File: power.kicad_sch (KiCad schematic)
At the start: 36 parts, among them J1 39281023, J7 39281023, J8 675031020, U1 AMS1117-3.3, U5 TPS62933, U6 TPS62933

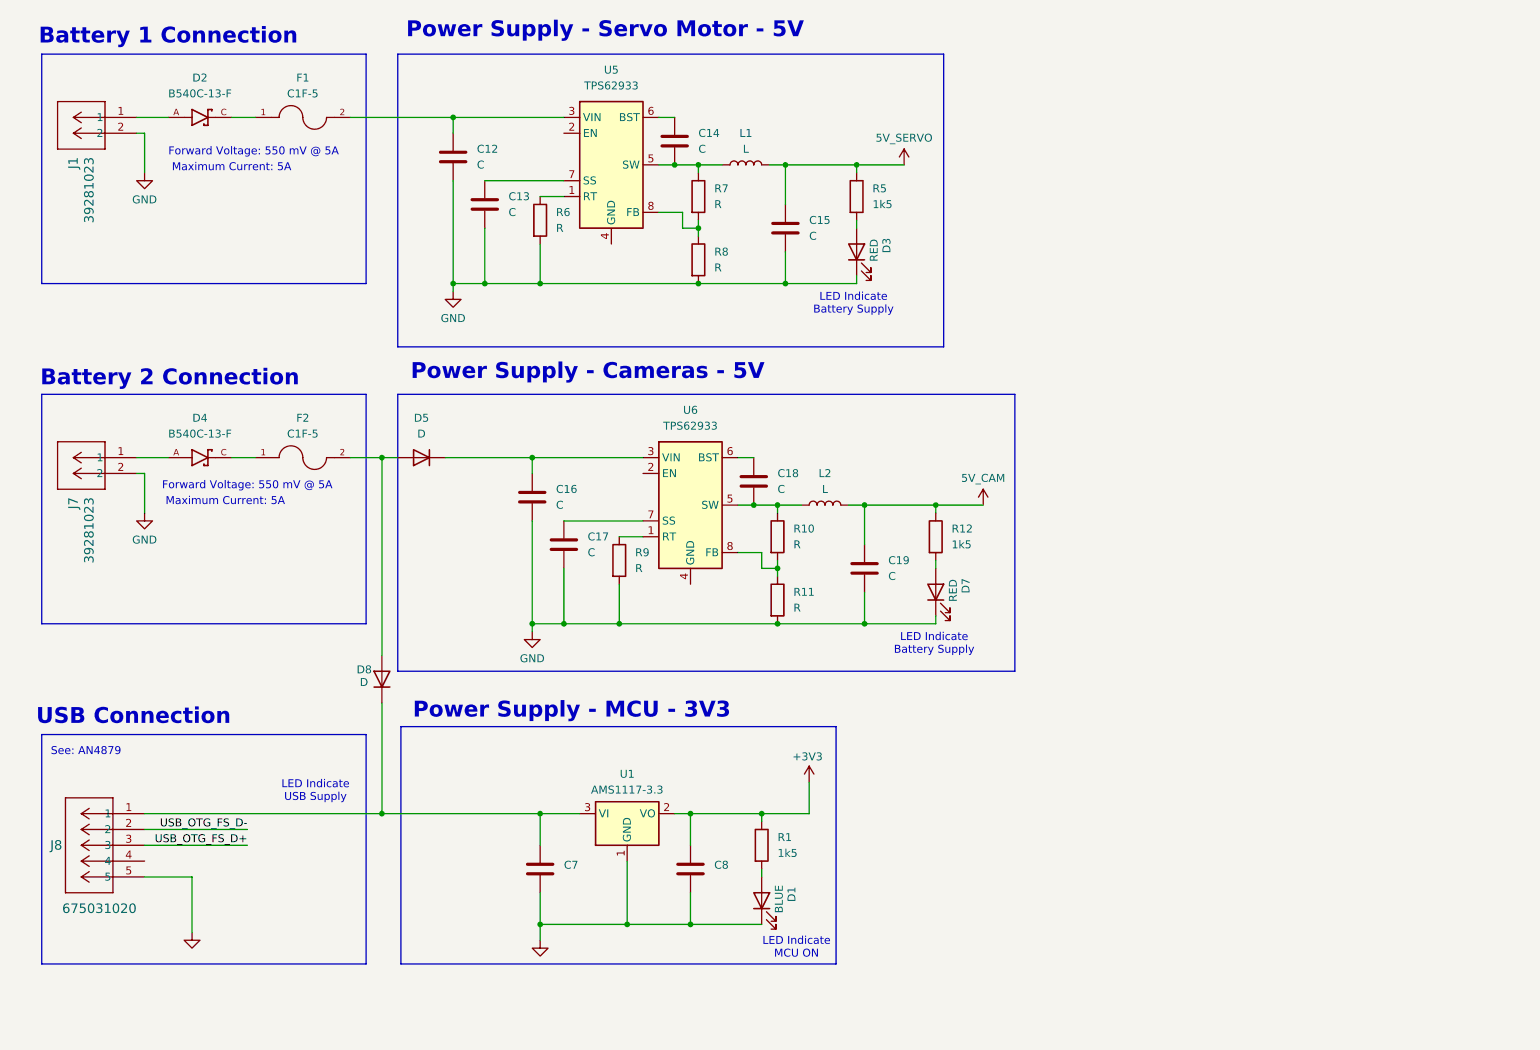
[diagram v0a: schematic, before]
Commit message: Remove redundant diode for camera supply
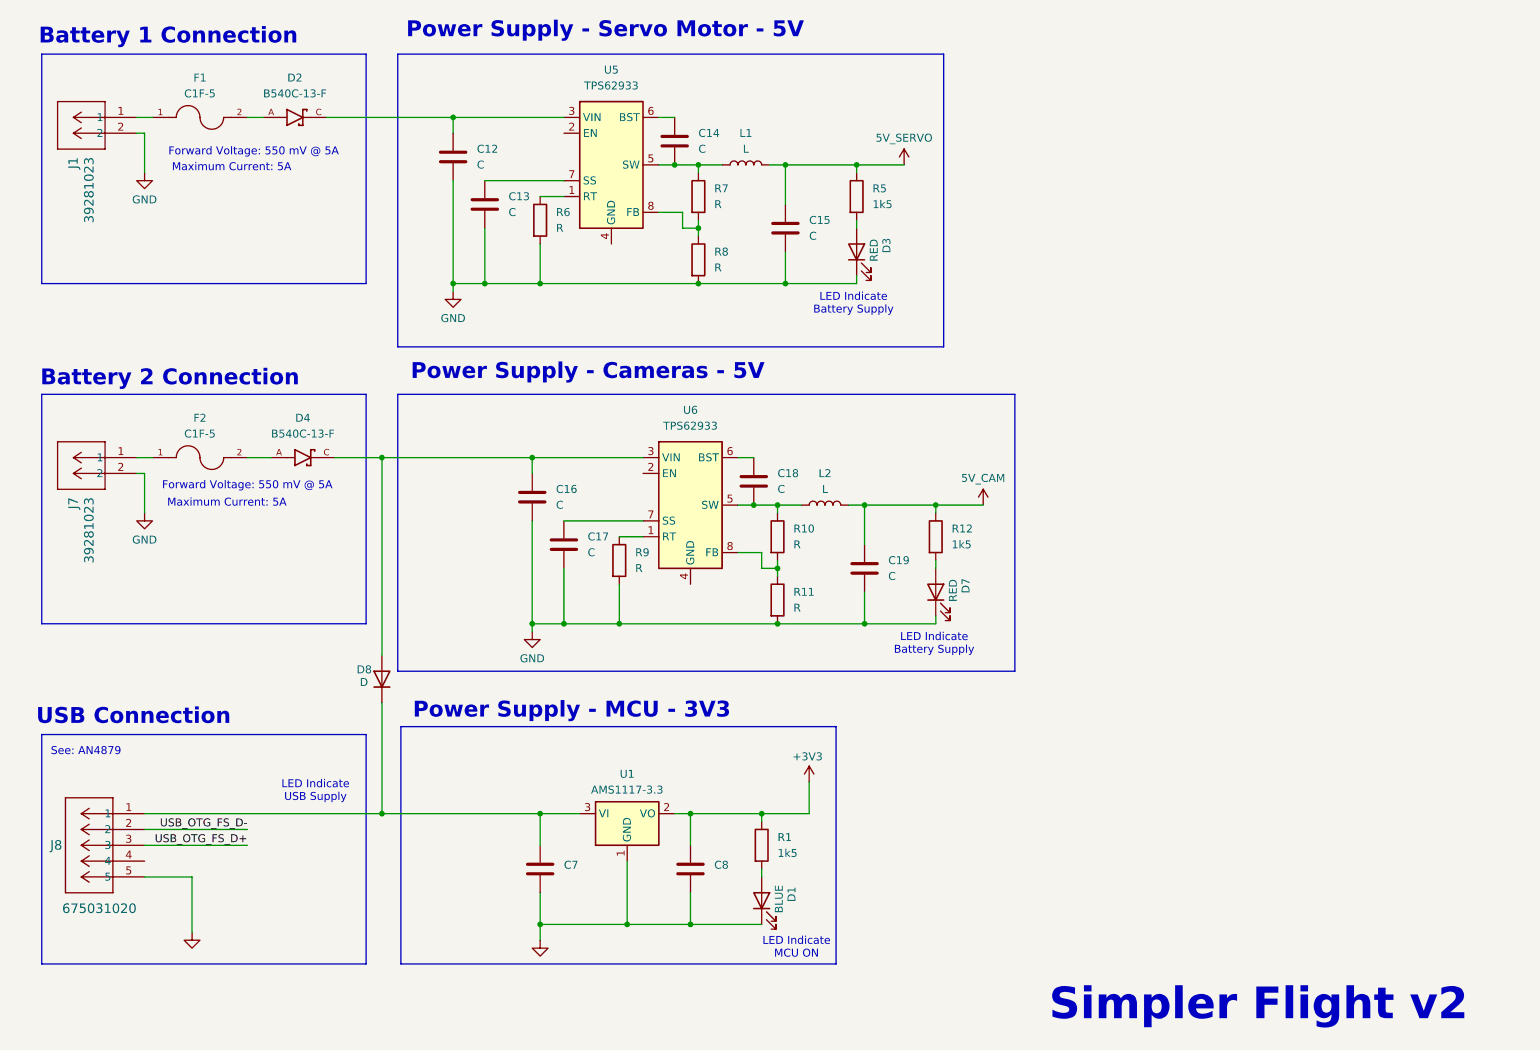
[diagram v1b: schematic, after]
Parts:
- removed D5: D, symbol Device:D
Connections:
- net at J7.1: now also F2.1; no longer D4.A
- net at C16.1, U6.3 (VIN): now also D4.C, D8.2 (A)
- net at D2.A: now also F1.2; no longer J1.1
- net at D2.C: now also C12.1, U5.3 (VIN); no longer F1.1
- net at F2.2: now also D4.A; no longer D8.2 (A)
- new net: F1.1, J1.1
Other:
- note added: "Simpler Flight v2"
- company: (none) -> Lulu Systems
- title: (none) -> Power System
- moved on the sheet: D2, D4, F1, F2

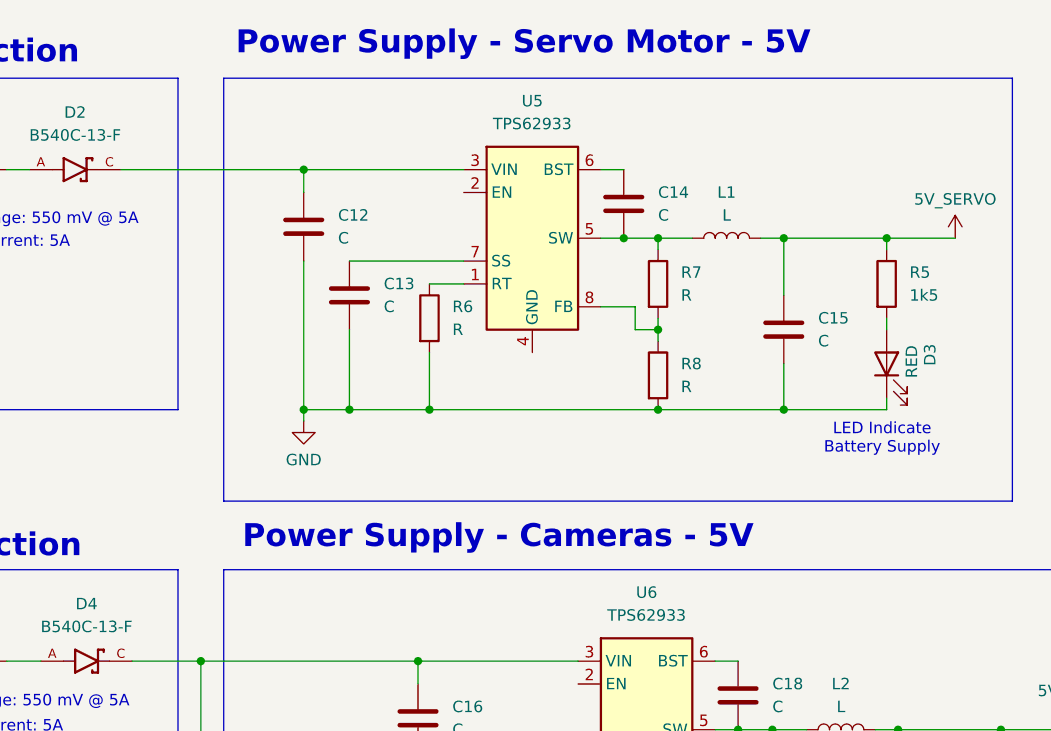
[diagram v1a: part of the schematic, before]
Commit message: Upload architecture diagram, start sensor schematic, add simulation files
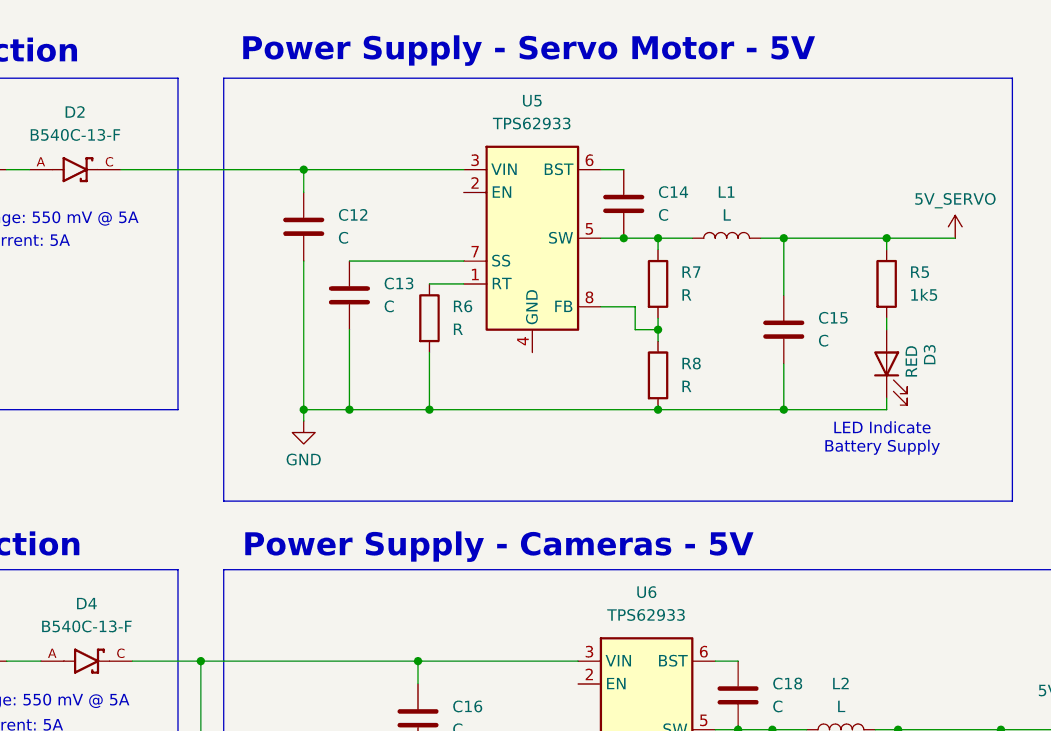
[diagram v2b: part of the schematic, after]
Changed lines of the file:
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@@
 	(text "Power Supply - Servo Motor - 5V"
 		(exclude_from_sim no)
-		(at 109.474 17.78 0)
+		(at 109.982 18.542 0)
 		(effects
 			(font
@@
 	(text "Power Supply - Cameras - 5V"
 		(exclude_from_sim no)
-		(at 106.68 72.644 0)
+		(at 106.68 73.66 0)
 		(effects
 			(font

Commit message: Commit
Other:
- title: Power System -> Power 
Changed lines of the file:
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@@
 	(paper "A4")
 	(title_block
-		(title "Power System")
+		(title "Power ")
 		(company "Lulu Systems")
 	)

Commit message: addecd stuff
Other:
- note added: "LED Indicate Battery Supply to Cameras"
- note added: "LED Indicate Battery Supply to Servo"
- note removed: "LED Indicate Battery Supply"
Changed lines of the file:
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@@
 		)
 	)
-	(text "LED Indicate \nBattery Supply\n\n"
+	(text "LED Indicate \nBattery Supply\nto Cameras"
 		(exclude_from_sim no)
 		(at 162.306 117.348 0)
@@
 		)
 	)
-	(text "LED Indicate \nBattery Supply\n\n"
+	(text "LED Indicate \nBattery Supply\nto Servo"
 		(exclude_from_sim no)
 		(at 149.352 62.738 0)
@@
 			"AAAAAAAAAAAAAAAAAAAAAAAAAAAAAAAAAAAAAAAAAAAAAAAAAAAAAAAAAAAAAAAAAAAAAAAAAAAA"
 			"AAAAAAAAAAAAAAAAAAAAAAAAAAAAAAAAAAAAAAAAAAAAAAAAAAAAAAAAAAAAAAAAAAAAAAAAAAAA"
+			"AAAAAAAAAAAAAAAAAAAAAAAAAAAAAAAAAAAAAAAAAAAAAAAAAAAAAAAAAAAAAAAAAAAAAAAAAAAA"
+			"AAAAAAAAAAAAAAAAAAAAAAAAAAAAAAAAAAAAAAAAAAAAAAAAAAAAAAAAAAAAAAAAAAAAAAAAAAAA"
+			"AAAAAAAAAAAAAAAAAAAAAAAAAAAAAAAAAAAAAAAAAAAAAAAAAAAAAAAAAAAAAAAAAAAAAAAAAAAA"
+			"AAAAAAAAAAAAAAAAAAAAAAAAAAAAAAAAAAAAAAAAAAAAAAAAAAAAAAAAAAAAAAAAAAAAAAAAAAAA"
+			"AAAAAAAAAAAAAAAAAAAAAAAAAAAAAAAAAAAAAAAAAAAAAAAAAAAAAAAAAAAAAAAAAAAAAAAAAAAA"
+			"AAAAAAAAAAAAAAAAAAAAAAAAAAAAAAAAAAAAAAAAAAAAAAAAAAAAAAAAAAAAAAAAAAAAAAAAAAAA"
+			"AAAAAAAAAAAAAAAAAAAAAAAAAAAAAAAAAAAAAAAAAAAAAAAAAAAAAAAAAAAAAAAAAAAAAAAAAAAA"
+			"AAAAAAAAAAAAAAAAAAAAAAAAAAAAAAAAAAAAAAAAAAAAAAAAAAAAAAAAAAAAAAAAAAAAAAAAAAAA"
+			"AAAAAAAAAAAAAAAAAAAAAAAAAAAAAAAAAAAAAAAAAAAAAAAAAAAAAAAAAAAAAAAAAAAAAAAAAAAA"
+			"AAAAAAAAAAAAAAAAAAAAAAAAAAAAAAAAAAAAAAAAAAAAAAAAAAAAAAAAAAAAAAAAAAAAAAAAAAAA"
+			"AAAAAAAAAAAAAAAAAAAAAAAAAAAAAAAAAAAAAAAAAAAAAAAAAAAAAAAAAAAAAAAAAAAAAAAAAAAA"
+			"AAAAAAAAAAAAAAAAAAAAAAAAAAAAAAAAAAAAAAAAAAAAAAAAAAAAAAAAAAAAAAAAAAAAAAAAAAAA"
+			"AAAAAAAAAAAAAAAAAAAAAAAAAAAAAAAAAAAAAAAAAAAAAAAAAAAAAAAAAAAAAAAAAAAAAAAAAAAA"
+			"AAAAAAAAAAAAAAAAAAAAAAAAAAAAAAAAAAAAAAAAAAAAAAAAAAAAAAAAAAAAAAAAAAAAAAAAAAAA"
+			"AAAAAAAAAAAAAAAAAAAAAAAAAAAAAAAAAAAAAAAAAAAAAAAAAAAAAAAAAAAAAAAAAAAAAAAAAAAA"
+			"AAAAAAAAAAAAAAAAAAAAAAAAAAAAAAAAAAAAAAAAAAAAAAAAAAAAAAAAAAAAAAAAAAAAAAAAAAAA"
+			"AAAAAAAAAAAAAAAAAAAAAAAAAAAAAAAAAAAAAAAAAAAAAAAAAAAAAAAAAAAAAAAAAAAAAAAAAAAA"
+			"AAAAAAAAAAAAAAAAAAAAAAAAAAAAAAAAAAAAAAAAAAAAAAAAAAAAAAAAAAAAAAAAAAAAAAAAAAAA"

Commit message: Initiliase main components
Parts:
- C12, C13, C14, C15, C16, C17, C18, C19: footprint (none) -> Capacitor_SMD:C_0805_2012Metric
- D2, D4: footprint B540C-13-F:DIOM6959X245N -> B540C_13_F:DIOM6959X245N
- D8: footprint (none) -> Diode_SMD:D_0805_2012Metric_Pad1.15x1.40mm_HandSolder
- F1, F2: footprint C1F-5:FUSC3215X83N -> C1F_5:FUSC3215X83N
- J1: value 39281023 -> Battery 1
- J7: value 39281023 -> Battery 2
- J8: value 675031020 -> USB
- L1, L2: footprint (none) -> Inductor_SMD:L_0805_2012Metric
- R10, R11, R6, R7, R8, R9: footprint (none) -> Resistor_SMD:R_0805_2012Metric_Pad1.20x1.40mm_HandSolder
- R12: footprint Capacitor_SMD:C_0805_2012Metric -> Resistor_SMD:R_0805_2012Metric_Pad1.20x1.40mm_HandSolder
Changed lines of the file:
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@@
 			)
 		)
-		(property "Footprint" ""
+		(property "Footprint" "Inductor_SMD:L_0805_2012Metric"
 			(at 144.78 93.98 0)
 			(effects
@@
 			)
 		)
-		(property "Value" "39281023"
+		(property "Value" "Battery 2"
 			(at 26.6699 92.71 90)
 			(effects
@@
 			)
 		)
-		(property "Footprint" ""
+		(property "Footprint" "Capacitor_SMD:C_0805_2012Metric"
 			(at 98.7552 96.52 0)
 			(effects
@@
 			)
 		)
-		(property "Footprint" ""
+		(property "Footprint" "Capacitor_SMD:C_0805_2012Metric"
 			(at 103.8352 104.14 0)
 			(effects
@@
 			)
 		)
-		(property "Footprint" ""
+		(property "Footprint" "Resistor_SMD:R_0805_2012Metric_Pad1.20x1.40mm_HandSolder"
 			(at 135.382 109.22 90)
 			(effects
@@
 			)
 		)
-		(property "Footprint" "B540C-13-F:DIOM6959X245N"
+		(property "Footprint" "B540C_13_F:DIOM6959X245N"
 			(at 59.69 31.75 0)
 			(effects
@@
 			)
 		)
-		(property "Footprint" ""
+		(property "Footprint" "Inductor_SMD:L_0805_2012Metric"
 			(at 132.08 39.37 0)
 			(effects
@@
 			)
 		)
-		(property "Footprint" "B540C-13-F:DIOM6959X245N"
+		(property "Footprint" "B540C_13_F:DIOM6959X245N"
 			(at 60.96 86.36 0)
 			(effects
@@
 			)
 		)
-		(property "Footprint" ""
+		(property "Footprint" "Resistor_SMD:R_0805_2012Metric_Pad1.20x1.40mm_HandSolder"
 			(at 97.282 48.26 90)
 			(effects
@@
 			)
 		)
-		(property "Value" "675031020"
+		(property "Value" "USB"
 			(at 34.29 158.75 0)
 			(effects
@@
 			)
 		)
-		(property "Footprint" ""
+		(property "Footprint" "Capacitor_SMD:C_0805_2012Metric"
 			(at 91.1352 49.53 0)
 			(effects
@@
 			)
 		)
-		(property "Footprint" "Capacitor_SMD:C_0805_2012Metric"
+		(property "Footprint" "Resistor_SMD:R_0805_2012Metric_Pad1.20x1.40mm_HandSolder"
 			(at 160.782 99.06 90)
 			(effects
@@
 			)
 		)
-		(property "Footprint" ""
+		(property "Footprint" "Capacitor_SMD:C_0805_2012Metric"
 			(at 139.3952 53.34 0)
 			(effects
@@
 			)
 		)
-		(property "Footprint" "C1F-5:FUSC3215X83N"
+		(property "Footprint" "C1F_5:FUSC3215X83N"
 			(at 44.45 86.36 0)
 			(effects
@@
 			)
 		)
-		(property "Footprint" ""
+		(property "Footprint" "Capacitor_SMD:C_0805_2012Metric"
 			(at 134.3152 93.98 0)
 			(effects
@@
 			)
 		)
-		(property "Footprint" ""
+		(property "Footprint" "Resistor_SMD:R_0805_2012Metric_Pad1.20x1.40mm_HandSolder"
 			(at 122.682 44.45 90)
 			(effects
@@
 			)
 		)
-		(property "Footprint" ""
+		(property "Footprint" "Resistor_SMD:R_0805_2012Metric_Pad1.20x1.40mm_HandSolder"
 			(at 109.982 102.87 90)
 			(effects
@@
 			)
 		)
-		(property "Value" "39281023"
+		(property "Value" "Battery 1"
 			(at 26.6699 38.1 90)
 			(effects
@@
 			)
 		)
-		(property "Footprint" ""
+		(property "Footprint" "Diode_SMD:D_0805_2012Metric_Pad1.15x1.40mm_HandSolder"
 			(at 73.66 121.92 0)
 			(effects
@@
 			)
 		)
-		(property "Footprint" ""
+		(property "Footprint" "Resistor_SMD:R_0805_2012Metric_Pad1.20x1.40mm_HandSolder"
 			(at 135.382 99.06 90)
 			(effects
@@
 			)
 		)
-		(property "Footprint" ""
+		(property "Footprint" "Capacitor_SMD:C_0805_2012Metric"
 			(at 152.0952 107.95 0)
 			(effects
@@
 			)
 		)
-		(property "Footprint" ""
+		(property "Footprint" "Resistor_SMD:R_0805_2012Metric_Pad1.20x1.40mm_HandSolder"
 			(at 122.682 54.61 90)
 			(effects
@@
 			)
 		)
-		(property "Footprint" ""
+		(property "Footprint" "Capacitor_SMD:C_0805_2012Metric"
 			(at 121.6152 39.37 0)
 			(effects
@@
 			)
 		)
-		(property "Footprint" ""
+		(property "Footprint" "Capacitor_SMD:C_0805_2012Metric"
 			(at 86.0552 41.91 0)
 			(effects
@@
 			)
 		)
-		(property "Footprint" "C1F-5:FUSC3215X83N"
+		(property "Footprint" "C1F_5:FUSC3215X83N"
 			(at 44.45 31.75 0)
 			(effects
